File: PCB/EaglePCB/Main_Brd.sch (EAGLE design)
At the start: 71 parts, among them J2 702461401, U1 ATWINC1500-MR210PB1952-T, U3 MSP430FR2355TDBTRDBT0038A_M, U6 ARJM11C7-114-BA-EW2

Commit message: finished pcb v1
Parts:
- added U$8: MAGICWIFI_X10, 473:MAGICWIFI_X10
- renumbered J2 to TI-JTAG
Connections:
- new net LORA1_IRQ2: LORA1.DIO1, U3.P3.2_OA2-
- new net LORA2_IRQ2: LORA2.DIO1, U3.P2.5_COMP1.0
- net !ATC_RST: now also U3.P2.3_TB1TRG; no longer U3.P3.2_OA2-
- net ATC_EN: now also U3.P2.6_MCLK_XOUT

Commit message: Final Revision V1.1 for Print
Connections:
- new net 3.3: U3.P3.3_OA2+
- new net 3.5: U3.P3.5_OA3O
- new net 3.6: U3.P3.6_OA3-
- new net 3.7: U3.P3.7_OA3+
- new net 5.0: U3.P5.0_TB2.1_MFM.RX_A8
- new net 5.1: U3.P5.1_TB2.2_MFM.TX_A9

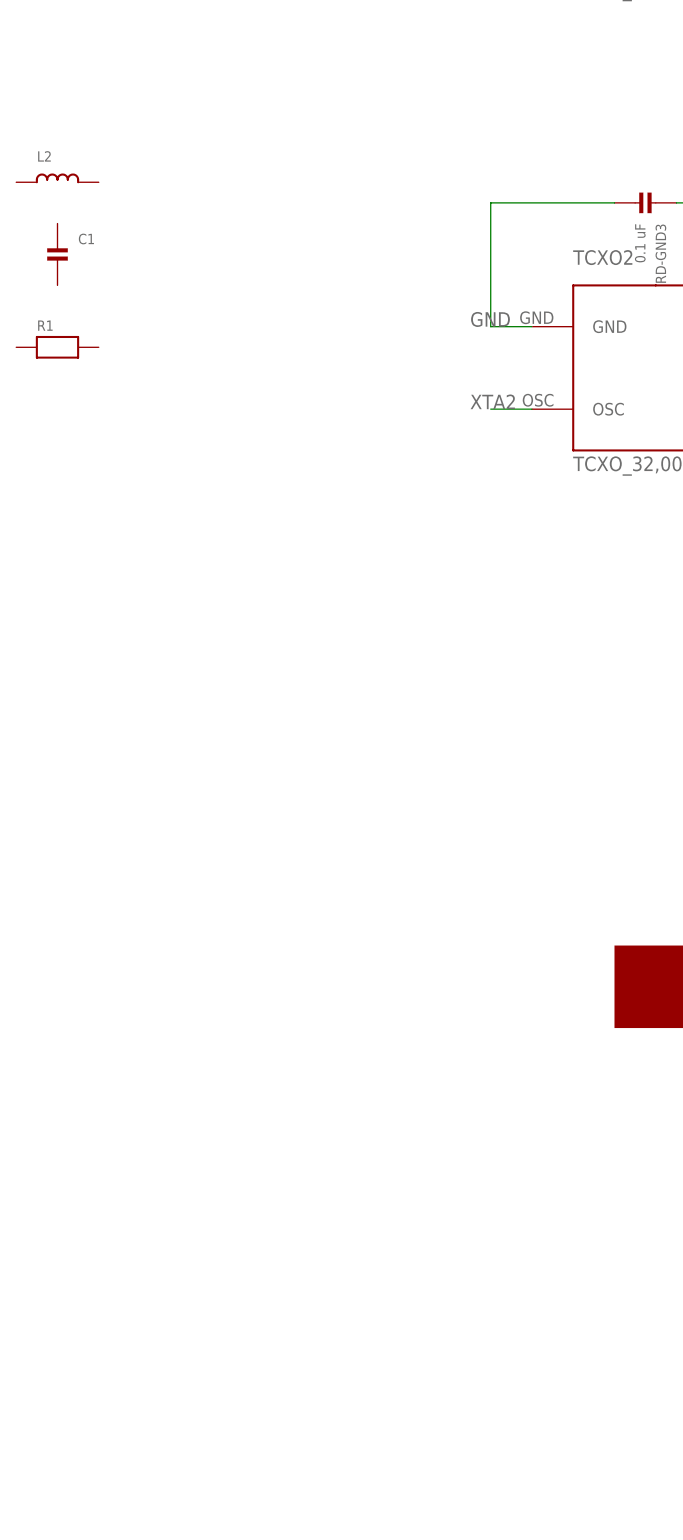
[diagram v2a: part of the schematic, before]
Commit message: fixed top ground plane issue
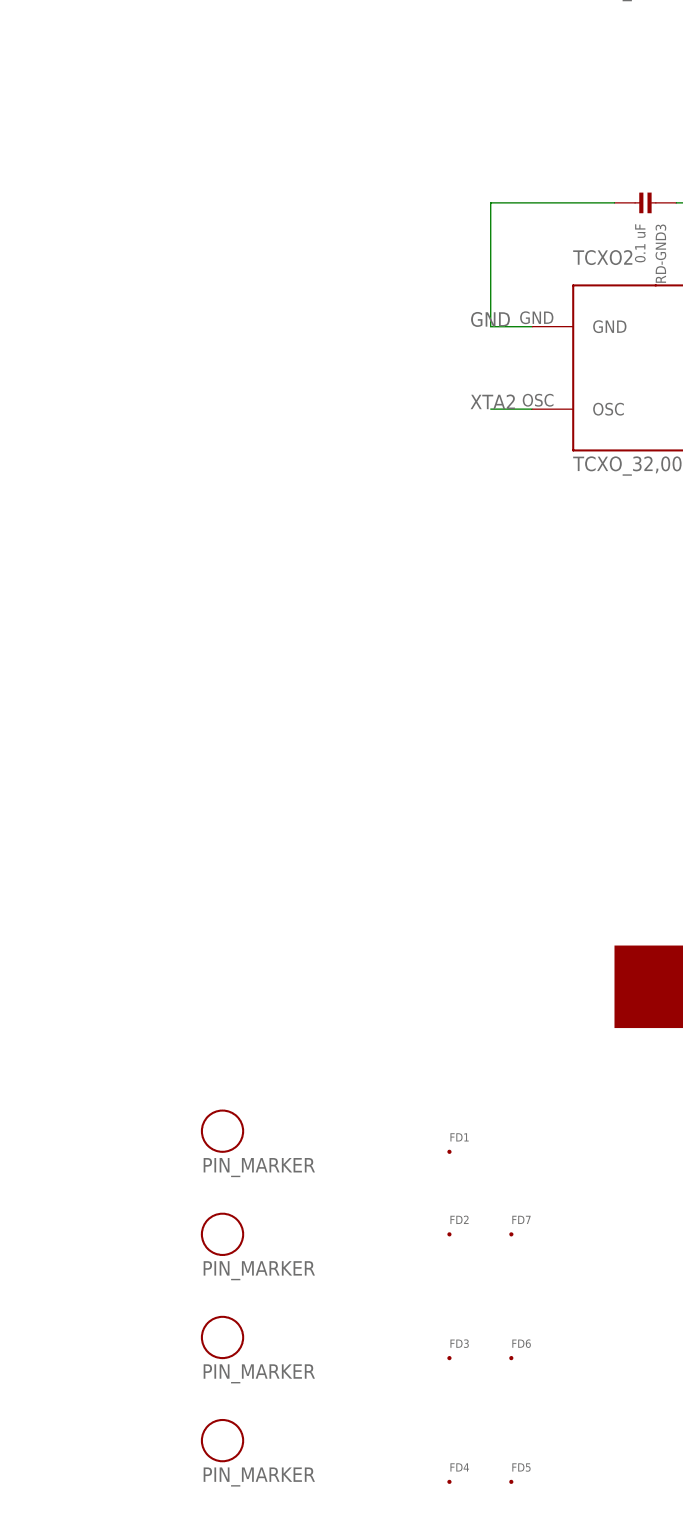
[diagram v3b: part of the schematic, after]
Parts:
- removed C1: (no value), microbuilder:CAP_CERAMIC0402
- removed L2: (no value), microbuilder:INDUCTOR_0402
- removed R1: (no value), microbuilder:RESISTOR0402
- added FD1, FD2, FD3, FD4, FD5, FD6, FD7: FID_40MIL, Fiducial:FID_40MIL
- added U$10, U$11, U$12, U$9: PIN_MARKER, 473:PIN_MARKER
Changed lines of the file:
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@@
 <?xml version="1.0" encoding="utf-8"?>
 <!DOCTYPE eagle SYSTEM "eagle.dtd">
-<eagle version="9.7.0">
+<eagle version="9.6.2">
 <drawing>
 <settings>
@@
 <layer number="59" name="tCarbon" color="7" fill="1" visible="no" active="no"/>
 <layer number="60" name="bCarbon" color="7" fill="1" visible="no" active="no"/>
-<layer number="88" name="SimResults" color="9" fill="1" visible="yes" active="yes"/>
+<layer number="88" name="SimResults" color="9" fill="1" visible="no" active="yes"/>
 <layer number="89" name="SimProbes" color="9" fill="1" visible="yes" active="yes"/>
 <layer number="90" name="Modules" color="5" fill="1" visible="yes" active="yes"/>
@@
 <part name="VR_PA-PA_BOOST" library="microbuilder" deviceset="INDUCTOR" device="_0402" value="33nH"/>
 <part name="RFO-33PF" library="microbuilder" deviceset="INDUCTOR" device="_0402" value="10nH"/>
-<part name="L2" library="microbuilder" deviceset="INDUCTOR" device="_0402"/>
-<part name="C1" library="microbuilder" deviceset="CAP_CERAMIC" device="0402"/>
-<part name="R1" library="microbuilder" deviceset="RESISTOR" device="0402"/>
 <part name="10NH-ANT1" library="microbuilder" deviceset="CAP_CERAMIC" device="0402"/>
 <part name="ANT1-GND" library="microbuilder" deviceset="CAP_CERAMIC" device="0402" value="4.7pF"/>
@@
 <part name="U$7" library="473" deviceset="BARREL_CONN_EXTERN" device=""/>
 <part name="U$8" library="473" library_urn="urn:adsk.wipprod:fs.file:vf.lBtoW6XlTqmMxyMuKqhWUA" deviceset="MAGICWIFI_X10" device="" value="MAGICWIFI_X10"/>
+<part name="U$9" library="473" deviceset="PIN_MARKER" device=""/>
+<part name="U$10" library="473" deviceset="PIN_MARKER" device=""/>
+<part name="U$11" library="473" deviceset="PIN_MARKER" device=""/>
+<part name="U$12" library="473" deviceset="PIN_MARKER" device=""/>
+<part name="FD1" library="Fiducial" deviceset="FID" device="_40MIL"/>
+<part name="FD2" library="Fiducial" deviceset="FID" device="_40MIL"/>
+<part name="FD3" library="Fiducial" deviceset="FID" device="_40MIL"/>
+<part name="FD4" library="Fiducial" deviceset="FID" device="_40MIL"/>
+<part name="FD5" library="Fiducial" deviceset="FID" device="_40MIL"/>
+<part name="FD6" library="Fiducial" deviceset="FID" device="_40MIL"/>
+<part name="FD7" library="Fiducial" deviceset="FID" device="_40MIL"/>
 </parts>
 <sheets>
@@
 <attribute name="VALUE" x="-40.64" y="195.58" size="1.27" layer="96"/>
 </instance>
-<instance part="L2" gate="G$1" x="-210.82" y="55.88" smashed="yes" grouprefs="0402">
-<attribute name="NAME" x="-213.36" y="58.42" size="1.27" layer="95"/>
-<attribute name="VALUE" x="-213.36" y="53.34" size="1.27" layer="96"/>
-</instance>
-<instance part="C1" gate="G$1" x="-210.82" y="45.72" smashed="yes" grouprefs="0402">
-<attribute name="NAME" x="-208.28" y="48.26" size="1.27" layer="95" font="vector"/>
-<attribute name="VALUE" x="-208.28" y="45.72" size="1.27" layer="96" font="vector"/>
-</instance>
-<instance part="R1" gate="G$1" x="-210.82" y="35.56" smashed="yes" grouprefs="0402">
-<attribute name="NAME" x="-213.36" y="37.592" size="1.27" layer="95" font="vector"/>
-<attribute name="VALUE" x="-213.36" y="32.385" size="1.27" layer="96" font="vector"/>
-</instance>
 <instance part="10NH-ANT1" gate="G$1" x="-50.8" y="198.12" smashed="yes" rot="R90" grouprefs="ANTENNA1">
 <attribute name="NAME" x="-53.34" y="200.66" size="1.27" layer="95" font="vector" rot="R90"/>
@@
 <instance part="U$7" gate="G$1" x="101.6" y="91.44" smashed="yes"/>
 <instance part="U$8" gate="G$1" x="-137.16" y="-43.18" smashed="yes"/>
+<instance part="U$9" gate="G$1" x="-190.5" y="-60.96" smashed="yes">
+<attribute name="VALUE" x="-193.04" y="-66.04" size="1.778" layer="96"/>
+</instance>
+<instance part="U$10" gate="G$1" x="-190.5" y="-73.66" smashed="yes">
+<attribute name="VALUE" x="-193.04" y="-78.74" size="1.778" layer="96"/>
+</instance>
+<instance part="U$11" gate="G$1" x="-190.5" y="-86.36" smashed="yes">
+<attribute name="VALUE" x="-193.04" y="-91.44" size="1.778" layer="96"/>
+</instance>
+<instance part="U$12" gate="G$1" x="-190.5" y="-99.06" smashed="yes">
+<attribute name="VALUE" x="-193.04" y="-104.14" size="1.778" layer="96"/>
+</instance>
+<instance part="FD1" gate="G$2" x="-162.56" y="-63.5" smashed="yes">
+<attribute name="NAME" x="-162.56" y="-62.23" size="1.016" layer="95" font="vector" ratio="12"/>
+</instance>
+<instance part="FD2" gate="G$2" x="-162.56" y="-73.66" smashed="yes">
+<attribute name="NAME" x="-162.56" y="-72.39" size="1.016" layer="95" font="vector" ratio="12"/>
+</instance>
+<instance part="FD3" gate="G$2" x="-162.56" y="-88.9" smashed="yes">
+<attribute name="NAME" x="-162.56" y="-87.63" size="1.016" layer="95" font="vector" ratio="12"/>
+</instance>
+<instance part="FD4" gate="G$2" x="-162.56" y="-104.14" smashed="yes">
+<attribute name="NAME" x="-162.56" y="-102.87" size="1.016" layer="95" font="vector" ratio="12"/>
+</instance>
+<instance part="FD5" gate="G$2" x="-154.94" y="-104.14" smashed="yes">
+<attribute name="NAME" x="-154.94" y="-102.87" size="1.016" layer="95" font="vector" ratio="12"/>
+</instance>
+<instance part="FD6" gate="G$2" x="-154.94" y="-88.9" smashed="yes">
+<attribute name="NAME" x="-154.94" y="-87.63" size="1.016" layer="95" font="vector" ratio="12"/>
+</instance>
+<instance part="FD7" gate="G$2" x="-154.94" y="-73.66" smashed="yes">
+<attribute name="NAME" x="-154.94" y="-72.39" size="1.016" layer="95" font="vector" ratio="12"/>
+</instance>
 </instances>
 <busses>
